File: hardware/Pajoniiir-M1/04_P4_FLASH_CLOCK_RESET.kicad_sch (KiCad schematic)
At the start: 21 parts, among them U2 W25Q128JVPIQ, Y1 ECS-400-10-37B2-CKY-TR

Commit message: hardware: bind core hierarchical ports to nets
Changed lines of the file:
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@@
   (wire (pts (xy 198.12 72.39) (xy 198.12 64.77)) (stroke (width 0) (type default)))
   (wire (pts (xy 198.12 64.77) (xy 193.675 64.77)) (stroke (width 0) (type default)))
-  (hierarchical_label "3V3_SYS" (shape input) (at 34.925 34.925 0) (effects (font (size 1.27 1.27))))
+  (hierarchical_label "3V3_SYS" (shape input) (at 55.245 38.1 0) (effects (font (size 1.27 1.27))))
   (symbol
     (lib_id "Device:R_US") (at 55.245 41.91 0) (unit 1)
@@
     (instances (project "Pajoniiir-M1" (path "/2c8dd352-b7b8-4d9e-8f93-5dd43be2a100/31000004-6b2a-4a3a-8c91-000000000004" (reference "R_CHIP_PU") (unit 1))))
   )
-  (label "3V3_SYS" (at 55.245 38.1 0) (effects (font (size 1.27 1.27))))
   (label "CHIP_PU" (at 55.245 45.72 0) (effects (font (size 1.27 1.27))))
   (symbol

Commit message: hardware: connect flash and XTAL hierarchy stubs
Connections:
- net FLASH_VCC is gone; now on net FLASH_CS: C_FLASH.1, R_FLASH_CS.2, R_FLASH_CS_PU.1, R_FLASH_CS_PU.2, U2.4 (GND)
- net XTAL_P_NODE is gone; now on net XTAL_P: C_XTAL_P.1, R_XTAL_SER.2, Y1.1
- net FLASH_CK: now also R_FLASH_CLK.2, U2.7 (~{HOLD}/~{RESET}/IO_{3})
- net FLASH_D: now also R_FLASH_D0.2, U2.3 (~{WP}/IO_{2})
- net FLASH_HOLD: now also R_FLASH_D3.2, U2.6 (CLK)
- net FLASH_Q: now also R_FLASH_D1.2, U2.2 (DO/IO_{1})
- net FLASH_WP: now also R_FLASH_D2.2, U2.5 (DI/IO_{0})
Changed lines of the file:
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@@
     (comment 2 "Crystal caps 15pF are EVT start values")
   )
+  (wire (pts (xy 100.33 59.69) (xy 107.95 59.69)) (stroke (width 0) (type default)))
+  (wire (pts (xy 100.33 62.23) (xy 107.95 62.23)) (stroke (width 0) (type default)))
+  (wire (pts (xy 100.33 64.77) (xy 107.95 64.77)) (stroke (width 0) (type default)))
+  (wire (pts (xy 100.33 67.31) (xy 107.95 67.31)) (stroke (width 0) (type default)))
+  (wire (pts (xy 100.33 69.85) (xy 107.95 69.85)) (stroke (width 0) (type default)))
+  (wire (pts (xy 100.33 72.39) (xy 107.95 72.39)) (stroke (width 0) (type default)))
+  (wire (pts (xy 173.355 64.77) (xy 180.975 64.77)) (stroke (width 0) (type default)))
   (junction (at 111.76 72.39) (diameter 0) (color 0 0 0 0))
   (junction (at 184.15 64.77) (diameter 0) (color 0 0 0 0))

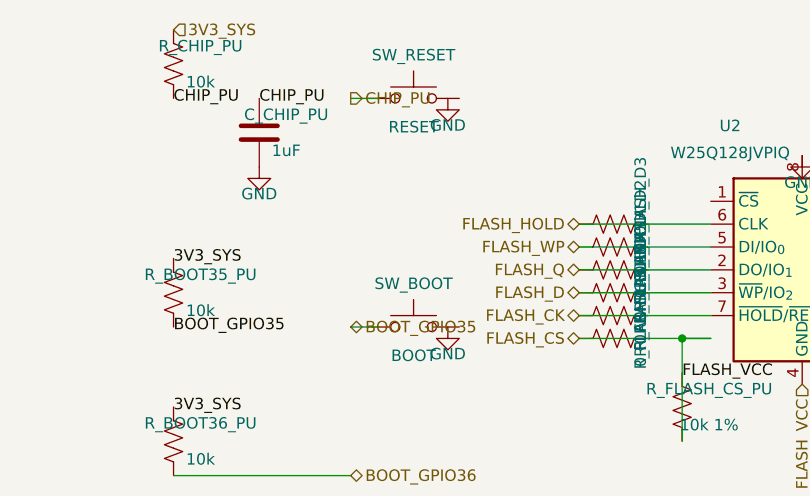
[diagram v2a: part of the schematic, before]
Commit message: hardware: terminate reset and boot switch nets
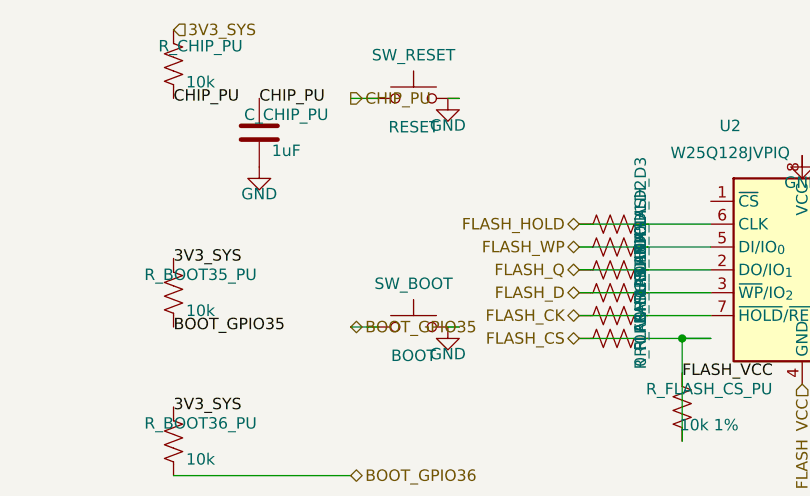
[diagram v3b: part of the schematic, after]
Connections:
- net BOOT_GPIO35: now also SW_BOOT.1
- net CHIP_PU: now also SW_RESET.1
- net GND: now also SW_BOOT.2, SW_RESET.2
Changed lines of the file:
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@@
     (instances (project "Pajoniiir-M1" (path "/2c8dd352-b7b8-4d9e-8f93-5dd43be2a100/31000004-6b2a-4a3a-8c91-000000000004" (reference "SW_RESET") (unit 1))))
   )
-  (wire (pts (xy 78.105 45.72) (xy 74.93 45.72)) (stroke (width 0) (type default)))
+  (wire (pts (xy 78.105 45.72) (xy 76.835 45.72)) (stroke (width 0) (type default)))
+  (wire (pts (xy 76.835 45.72) (xy 74.93 45.72)) (stroke (width 0) (type default)))
+  (wire (pts (xy 86.995 45.72) (xy 85.725 45.72)) (stroke (width 0) (type default)))
   (symbol
     (lib_id "power:GND") (at 85.725 45.72 0) (unit 1)
@@
     (instances (project "Pajoniiir-M1" (path "/2c8dd352-b7b8-4d9e-8f93-5dd43be2a100/31000004-6b2a-4a3a-8c91-000000000004" (reference "SW_BOOT") (unit 1))))
   )
-  (wire (pts (xy 78.105 71.12) (xy 74.93 71.12)) (stroke (width 0) (type default)))
+  (wire (pts (xy 78.105 71.12) (xy 76.835 71.12)) (stroke (width 0) (type default)))
+  (wire (pts (xy 76.835 71.12) (xy 74.93 71.12)) (stroke (width 0) (type default)))
+  (wire (pts (xy 86.995 71.12) (xy 85.725 71.12)) (stroke (width 0) (type default)))
   (symbol
     (lib_id "power:GND") (at 85.725 71.12 0) (unit 1)

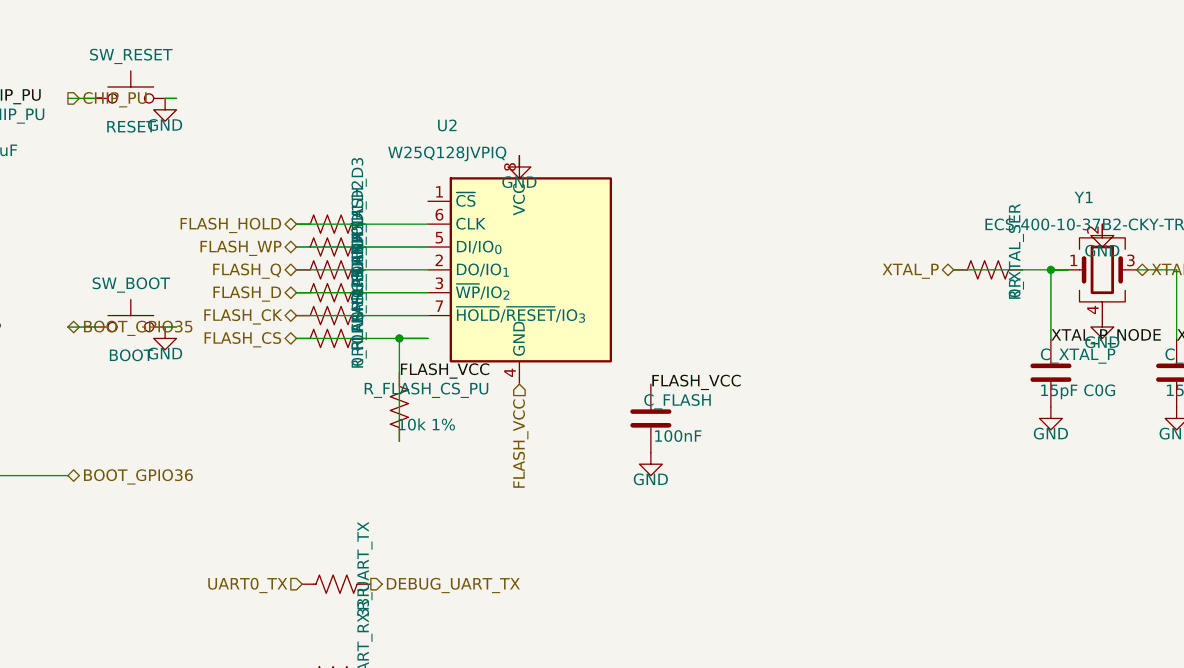
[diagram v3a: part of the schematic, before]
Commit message: hardware: correct W25Q flash signal and power mapping
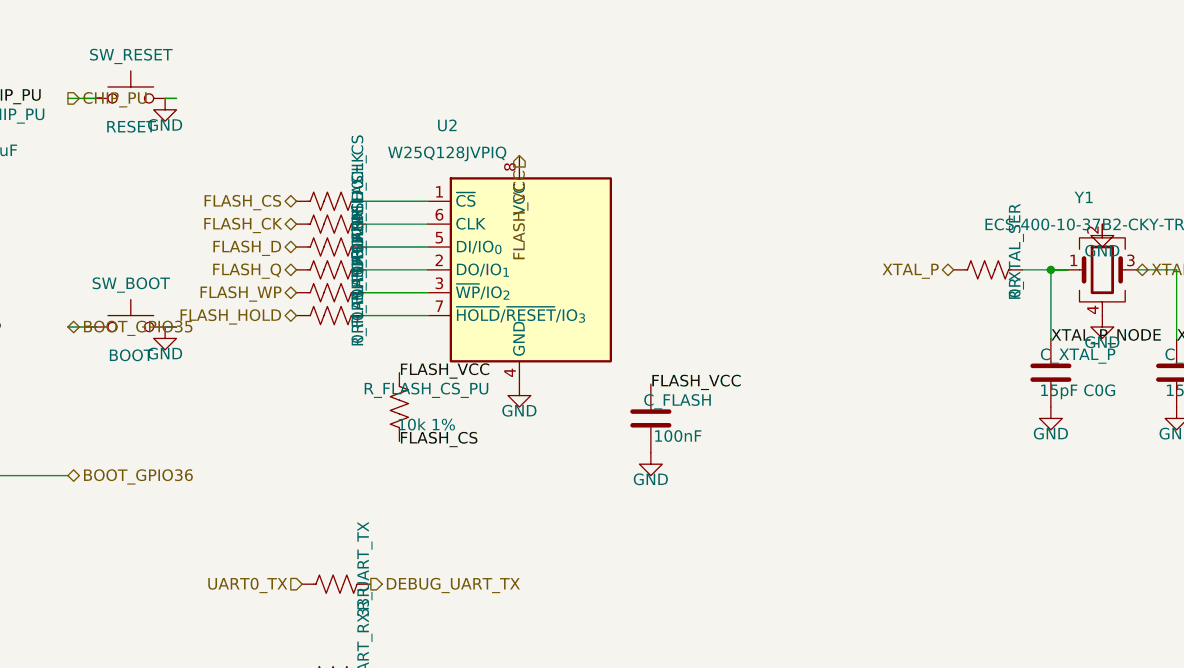
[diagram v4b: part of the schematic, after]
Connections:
- net FLASH_CK: no longer R_FLASH_CLK.2, U2.7 (~{HOLD}/~{RESET}/IO_{3})
- net FLASH_CS: no longer C_FLASH.1, R_FLASH_CS.2, R_FLASH_CS_PU.1, U2.4 (GND)
- net FLASH_D: no longer R_FLASH_D0.2, U2.3 (~{WP}/IO_{2})
- net FLASH_HOLD: no longer R_FLASH_D3.2, U2.6 (CLK)
- net FLASH_Q: no longer R_FLASH_D1.2, U2.2 (DO/IO_{1})
- net FLASH_WP: no longer R_FLASH_D2.2, U2.5 (DI/IO_{0})
- net GND: now also U2.4 (GND); no longer U2.8 (VCC)
- net XTAL_P: no longer C_XTAL_P.1, R_XTAL_SER.2, Y1.1
- net at U2.1 (~{CS}): now also R_FLASH_CS.2
- new net: R_FLASH_D1.2, U2.2 (DO/IO_{1})
- new net: R_FLASH_D2.2, U2.3 (~{WP}/IO_{2})
- new net: R_FLASH_D0.2, U2.5 (DI/IO_{0})
- new net: R_FLASH_CLK.2, U2.6 (CLK)
- new net: R_FLASH_D3.2, U2.7 (~{HOLD}/~{RESET}/IO_{3})
- new net FLASH_VCC: C_FLASH.1, R_FLASH_CS_PU.1, U2.8 (VCC)
- new net XTAL_P_NODE: C_XTAL_P.1, R_XTAL_SER.2, Y1.1
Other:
- moved on the sheet: R_FLASH_CLK, R_FLASH_CS, R_FLASH_D0, R_FLASH_D2, R_FLASH_D3

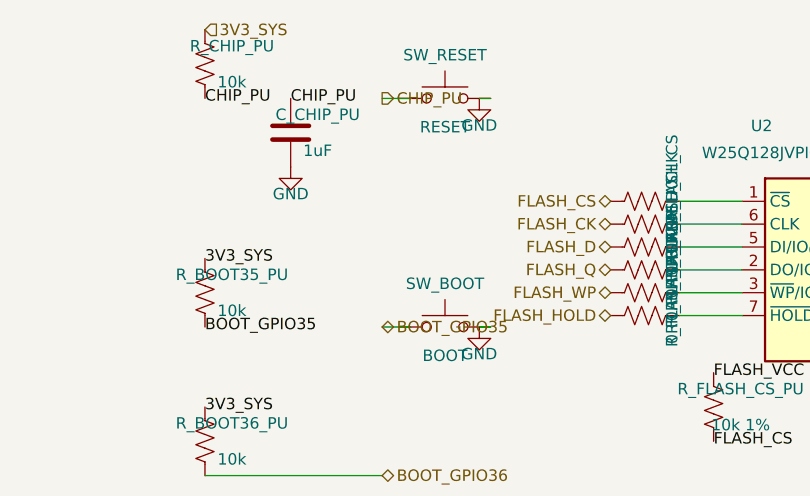
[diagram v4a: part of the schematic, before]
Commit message: hardware: remove stale reset and switched-rail wire stubs
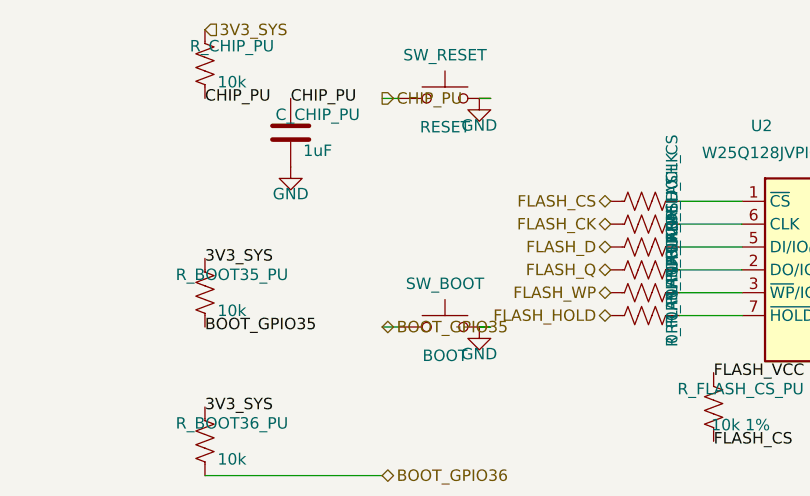
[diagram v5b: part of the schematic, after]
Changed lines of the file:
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@@
     (instances (project "Pajoniiir-M1" (path "/2c8dd352-b7b8-4d9e-8f93-5dd43be2a100/31000004-6b2a-4a3a-8c91-000000000004" (reference "SW_RESET") (unit 1))))
   )
-  (wire (pts (xy 78.105 45.72) (xy 76.835 45.72)) (stroke (width 0) (type default)))
   (wire (pts (xy 76.835 45.72) (xy 74.93 45.72)) (stroke (width 0) (type default)))
   (wire (pts (xy 86.995 45.72) (xy 85.725 45.72)) (stroke (width 0) (type default)))
@@
     (instances (project "Pajoniiir-M1" (path "/2c8dd352-b7b8-4d9e-8f93-5dd43be2a100/31000004-6b2a-4a3a-8c91-000000000004" (reference "SW_BOOT") (unit 1))))
   )
-  (wire (pts (xy 78.105 71.12) (xy 76.835 71.12)) (stroke (width 0) (type default)))
   (wire (pts (xy 76.835 71.12) (xy 74.93 71.12)) (stroke (width 0) (type default)))
   (wire (pts (xy 86.995 71.12) (xy 85.725 71.12)) (stroke (width 0) (type default)))
